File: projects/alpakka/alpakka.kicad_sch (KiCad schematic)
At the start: 56 parts, among them P1 Conn_01x20_Pin, P2 Conn_01x20_Pin, P3 Headers 4P IN, P4 Blade, P5 Jack 2.5mm, P6 Conn_01x02, U1 Alpsalpine_RKJXV, U10 ST_LSM6, U12 ST_LSM6, U2 Alpsalpine_RKJXV, U3 Alpsalpine_EC10E, U6 NXP_PCAL6416A, U8 NXP_PCAL6416A

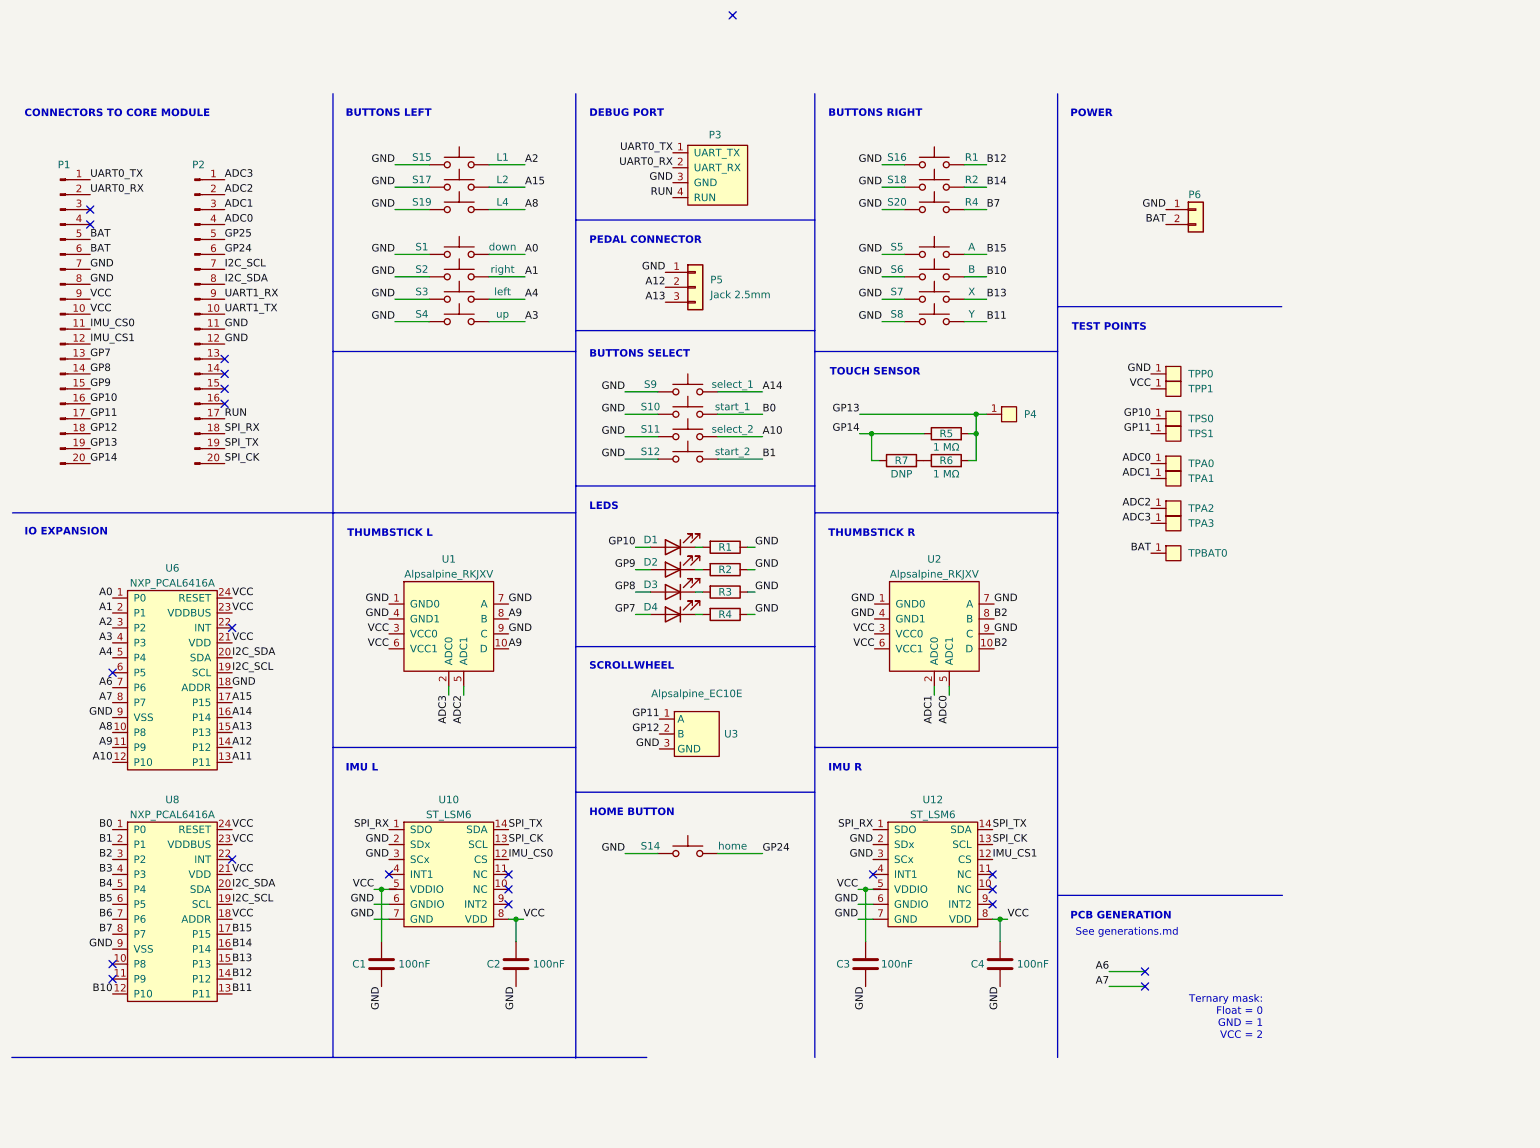
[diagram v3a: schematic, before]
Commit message: Alpakka added touch ref path, Reordered debug pins, Swapped analog 2-3, Removed wheel support holes, Added silkscreen
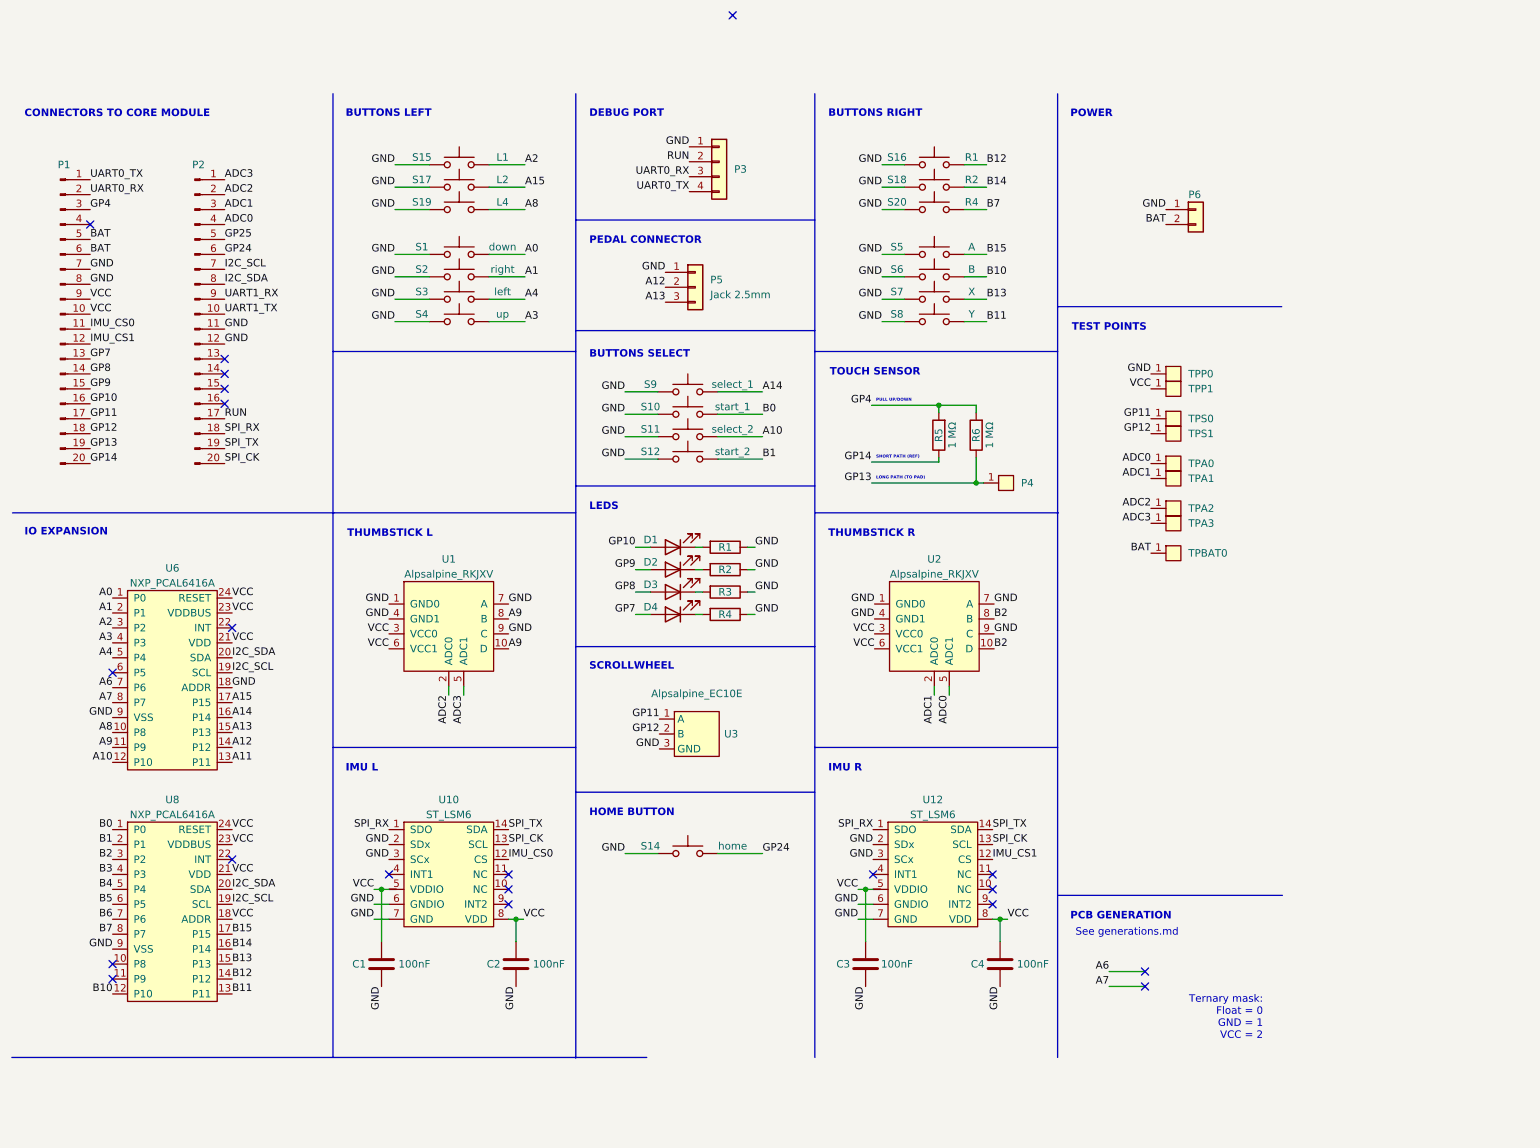
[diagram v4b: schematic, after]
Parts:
- removed P3: Headers 4P IN, ILO_fp:XKB_X6511FRS-04, symbol ILO_sym:Debug
- removed R7: DNP, ILO_fp:0603_compact, symbol Device:R
- added P3: Conn_01x04, ILO_fp:XKB_X6511FRS-04, symbol Connector_Generic:Conn_01x04
- renumbered R6 to R5, R5 to R6
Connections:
- net ADC2: now also U1.2 (ADC0); no longer U1.5 (ADC1)
- net ADC3: now also U1.5 (ADC1); no longer U1.2 (ADC0)
- net GND: now also P3.1 (Pin_1)
- net GP10: no longer TPS0.1
- net GP11: now also TPS0.1; no longer TPS1.1
- net GP12: now also TPS1.1
- net GP13: now also R6.1; no longer R5.2, R6.2
- net GP14: now also R5.1; no longer R6.1
- net RUN: now also P3.2 (Pin_2)
- net UART0_RX: now also P3.3 (Pin_3)
- net UART0_TX: now also P3.4 (Pin_4)
- net GP4: now reaches P1.3 (Pin_3)
- net GP4: now also R5.2, R6.2
- no-connect marks 22 -> 21
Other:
- note added: "LONG PATH (TO PAD)"
- note added: "PULL UP/DOWN"
- note added: "SHORT PATH (REF)"
- moved on the sheet: P4, R5, R6

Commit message: Alpakka revert to single touch path, Shifted GPIOs to match Marmota
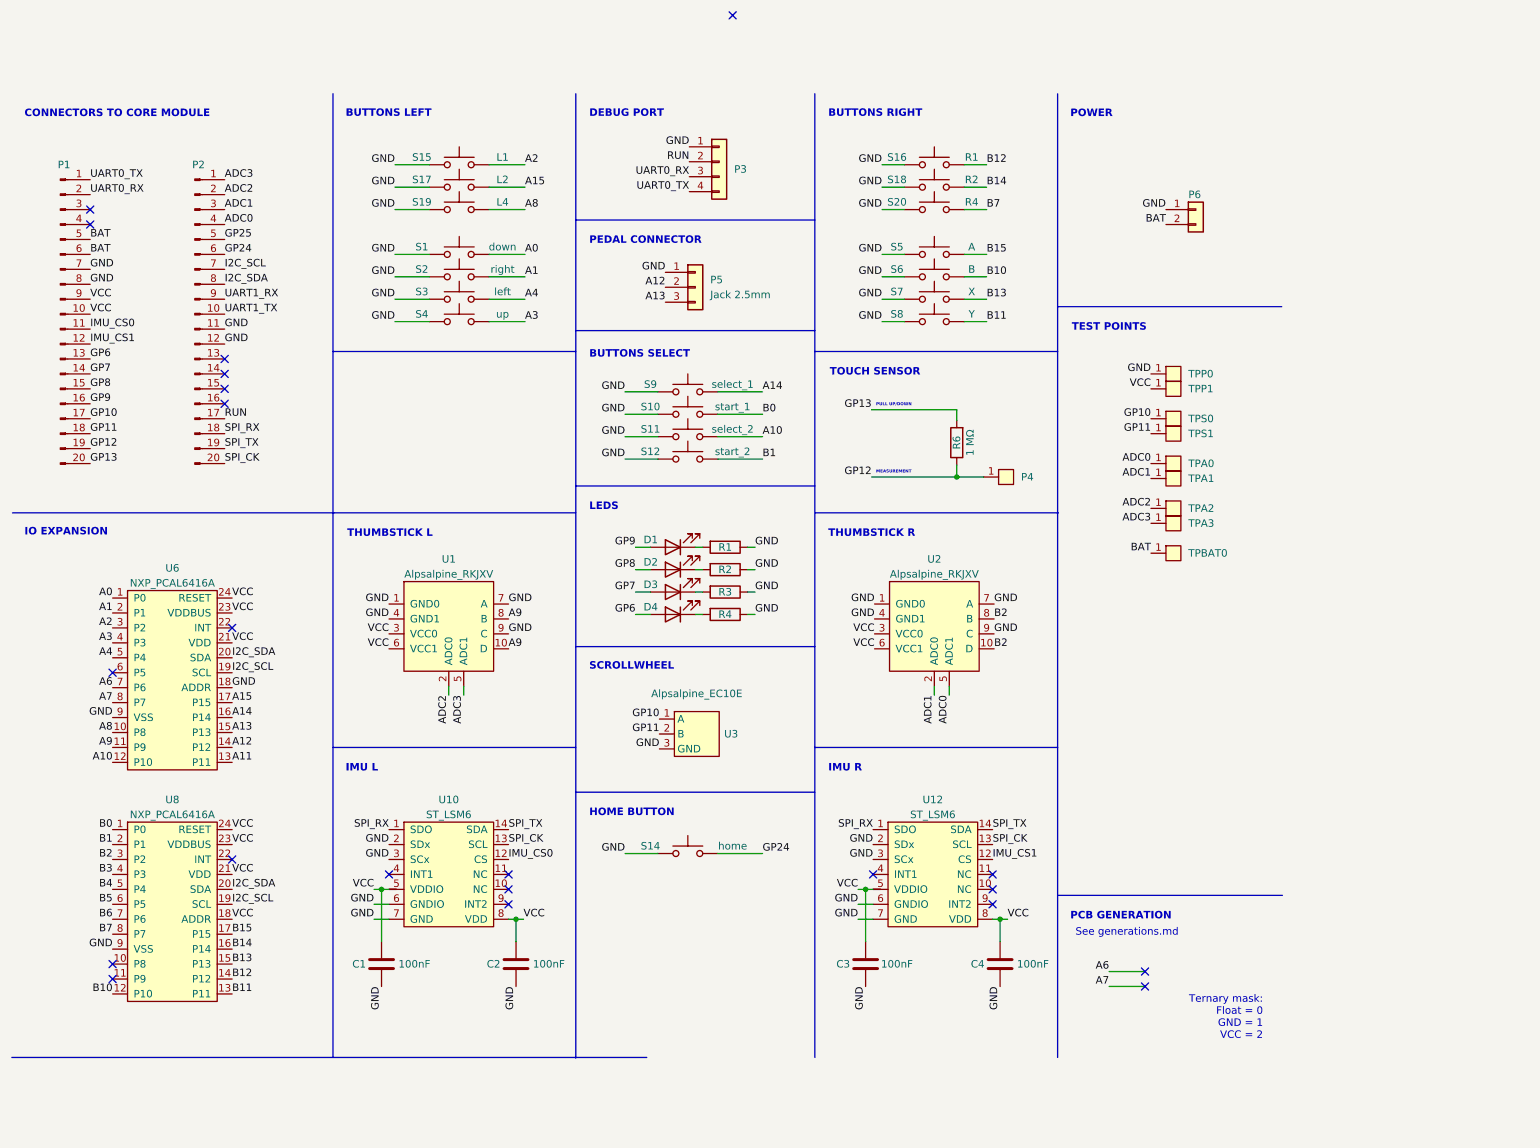
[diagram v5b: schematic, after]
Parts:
- removed R5: 1 MΩ, ILO_fp:0402, symbol Device:R
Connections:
- net GP14 is gone; now on net GP13: P1.20 (Pin_20)
- net GP10: now also P1.17 (Pin_17), TPS0.1, U3.1 (A); no longer D1.2 (A), P1.16 (Pin_16)
- net GP11: now also P1.18 (Pin_18), TPS1.1, U3.2 (B); no longer P1.17 (Pin_17), TPS0.1, U3.1 (A)
- net GP12: now also P1.19 (Pin_19), P4.1, R6.1; no longer P1.18 (Pin_18), TPS1.1, U3.2 (B)
- net GP13: now also R6.2; no longer P1.19 (Pin_19), P4.1, R6.1
- net GP7: now also D3.2 (A), P1.14 (Pin_14); no longer D4.2 (A), P1.13 (Pin_13)
- net GP8: now also D2.2 (A), P1.15 (Pin_15); no longer D3.2 (A), P1.14 (Pin_14)
- net GP9: now also D1.2 (A), P1.16 (Pin_16); no longer D2.2 (A), P1.15 (Pin_15)
- net GP4: no longer names the net of P1.3 (Pin_3)
- net GP4: no longer R6.2
- new net GP6: D4.2 (A), P1.13 (Pin_13)
- no-connect marks 21 -> 22
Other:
- note added: "MEASUREMENT"
- note removed: "LONG PATH (TO PAD)"
- note removed: "SHORT PATH (REF)"
- moved on the sheet: P4, R6

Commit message: Reworked Alpakka w/ interrupt lines, etc
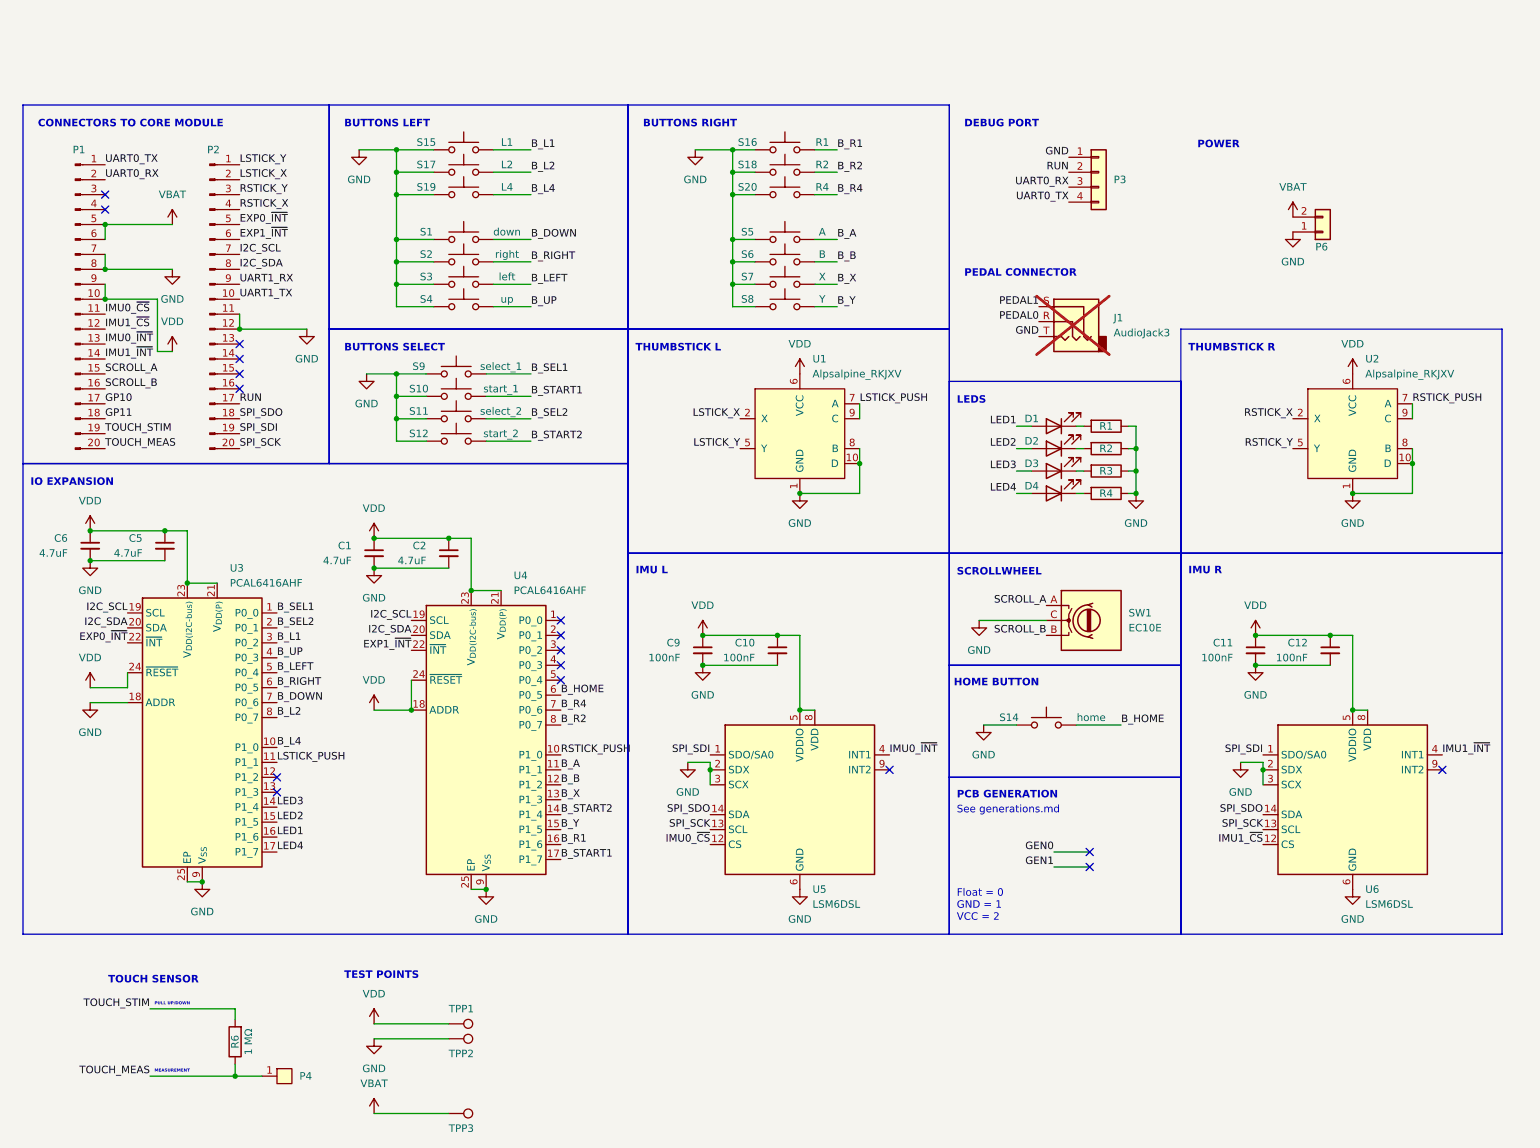
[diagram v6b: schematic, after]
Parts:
- removed C1, C2, C3, C4: 100nF, ILO_fp:0402, symbol Device:C
- removed P5: Jack 2.5mm, symbol Connector_Generic:Conn_01x03
- removed TPA0, TPA1, TPA2, TPA3, TPBAT0, TPP0, TPS0, TPS1: Endpoint, ILO_fp:Pad_1mm, symbol ILO_sym:Endpoint
- removed U10, U12: ST_LSM6, ILO_fp:LGA14, symbol ILO_sym:ST_LSM6
- removed U3: Alpsalpine_EC10E, ILO_fp:Alpsalpine_EC10E, symbol ILO_sym:Alpsalpine_EC10E
- removed U6, U8: NXP_PCAL6416A, ILO_fp:QFN24, symbol ILO_sym:NXP_PCAL6416A
- added C1, C2, C5, C6: 4.7uF, Capacitor_SMD:C_0603_1608Metric, symbol Device:C_Small
- added C10, C11, C12, C9: 100nF, Capacitor_SMD:C_0402_1005Metric, symbol Device:C_Small
- added J1: AudioJack3, Connector_Audio:Jack_3.5mm_CUI_SJ-3523-SMT_Horizontal, symbol Connector_Audio:AudioJack3
- added SW1: EC10E, ILO_fp:Alpsalpine_EC10E, symbol Device:RotaryEncoder
- added TPP2, TPP3: Endpoint, TestPoint:TestPoint_Pad_D1.0mm, symbol Connector:TestPoint
- added U3, U4: PCAL6416AHF, Package_DFN_QFN:HVQFN-24-1EP_4x4mm_P0.5mm_EP2.1x2.1mm, symbol Interface_Expansion:PCAL6416AHF
- added U5, U6: LSM6DSL, Package_LGA:LGA-14_3x2.5mm_P0.5mm_LayoutBorder3x4y, symbol Sensor_Motion:LSM6DSL
- D1, D2, D3, D4: footprint ILO_fp:0603_d -> Diode_SMD:D_0603_1608Metric
- P6: footprint ILO_fp:JST_PH_2_TH -> Connector_JST:JST_PH_S2B-PH-K_1x02_P2.00mm_Horizontal
- R1, R2, R3, R4: footprint ILO_fp:0603 -> Resistor_SMD:R_0603_1608Metric
- R6: footprint ILO_fp:0402 -> Resistor_SMD:R_0402_1005Metric
- TPP1: footprint ILO_fp:Pad_1mm -> TestPoint:TestPoint_Pad_D1.0mm; symbol ILO_sym:Endpoint -> Connector:TestPoint
- U1, U2: Export yes -> (none); Group Thumbstick -> (none); LCSC C918854 -> (none); Mount TH -> (none)
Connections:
- net A9 is gone; now on net GND: U1.10 (D), U1.8 (B)
- net B2 is gone; now on net GND: U2.10 (D), U2.8 (B)
- net GND: now also C1.2, C10.2, C11.2, C12.2, C2.2, C5.2, C6.2, C9.2, J1.T, SW1.C, TPP2.1, U3.18 (ADDR), U3.25 (EP), U3.9 (V_{SS}), U4.25 (EP), U4.9 (V_{SS}), U5.2 (SDX), U5.3 (SCX), U5.6 (GND), U5.7 (GND), U6.2 (SDX), U6.3 (SCX), U6.6 (GND), U6.7 (GND); no longer U1.7 (A), U1.9 (C), U2.7 (A), U2.9 (C)
- net I2C_SCL: now also U3.19 (SCL), U4.19 (SCL)
- net I2C_SDA: now also U3.20 (SDA), U4.20 (SDA)
- net A0 renamed B_DOWN
- net B_DOWN: now also U3.7 (P0_6)
- net A1 renamed B_RIGHT
- net B_RIGHT: now also U3.6 (P0_5)
- net A10 renamed B_SEL2
- net B_SEL2: now also U3.2 (P0_1)
- net A14 renamed B_SEL1
- net B_SEL1: now also U3.1 (P0_0)
- net A15 renamed B_L2
- net B_L2: now also U3.8 (P0_7)
- net A2 renamed B_L1
- net B_L1: now also U3.3 (P0_2)
- net A3 renamed B_UP
- net B_UP: now also U3.4 (P0_3)
- net A4 renamed B_LEFT
- net B_LEFT: now also U3.5 (P0_4)
- net A8 renamed B_L4
- net B_L4: now also U3.10 (P1_0)
- net ADC0 renamed RSTICK_X
- net RSTICK_X: now also U2.2 (X); no longer U2.5 (ADC1)
- net ADC1 renamed RSTICK_Y
- net RSTICK_Y: now also U2.5 (Y); no longer U2.2 (ADC0)
- net ADC2 renamed LSTICK_X
- net ADC3 renamed LSTICK_Y
- net B0 renamed B_START1
- net B_START1: now also U4.17 (P1_7)
- net B1 renamed B_START2
- net B_START2: now also U4.14 (P1_4)
- net B10 renamed B_B
- net B_B: now also U4.12 (P1_2)
- net B11 renamed B_Y
- net B_Y: now also U4.15 (P1_5)
- net B12 renamed B_R1
- net B_R1: now also U4.16 (P1_6)
- net B13 renamed B_X
- net B_X: now also U4.13 (P1_3)
- net B14 renamed B_R2
- net B_R2: now also U4.8 (P0_7)
- net B15 renamed B_A
- net B_A: now also U4.11 (P1_1)
- net B7 renamed B_R4
- net B_R4: now also U4.7 (P0_6)
- net BAT renamed VBAT
- net VBAT: now also TPP3.1
- net GP12 renamed TOUCH_MEAS
- net TOUCH_MEAS: now also P1.20 (Pin_20); no longer P1.19 (Pin_19)
- net GP13 renamed TOUCH_STIM
- net TOUCH_STIM: now also P1.19 (Pin_19); no longer P1.20 (Pin_20)
- net GP24 renamed B_HOME
- net B_HOME: now also U4.6 (P0_5); no longer P2.6 (Pin_6)
- net GP25 renamed EXP0_~{INT}
- net EXP0_~{INT}: now also U3.22 (~{INT})
- net GP6 renamed IMU0_~{INT}
- net IMU0_~{INT}: now also U5.4 (INT1); no longer D4.2 (A)
- net GP7 renamed IMU1_~{INT}
- net IMU1_~{INT}: now also U6.4 (INT1); no longer D3.2 (A)
- net GP8 renamed LED2
- net LED2: now also U3.15 (P1_5); no longer P1.15 (Pin_15)
- net GP9 renamed LED1
- net LED1: now also U3.16 (P1_6); no longer P1.16 (Pin_16)
- net IMU_CS0 renamed IMU0_~{CS}
- net IMU0_~{CS}: now also U5.12 (CS)
- net IMU_CS1 renamed IMU1_~{CS}
- net IMU1_~{CS}: now also U6.12 (CS)
- net SPI_CK renamed SPI_SCK
- net SPI_SCK: now also U5.13 (SCL), U6.13 (SCL)
- net SPI_RX renamed SPI_SDO
- net SPI_SDO: now also U5.14 (SDA), U6.14 (SDA)
- net SPI_TX renamed SPI_SDI
- net SPI_SDI: now also U5.1 (SDO/SA0), U6.1 (SDO/SA0)
- net VCC renamed VDD
- net VDD: now also C1.1, C10.1, C11.1, C12.1, C2.1, C5.1, C6.1, C9.1, U3.21 (V_{DD(P)}), U3.23 (V_{DD(I2C-bus)}), U3.24 (~{RESET}), U4.18 (ADDR), U4.21 (V_{DD(P)}), U4.23 (V_{DD(I2C-bus)}), U4.24 (~{RESET}), U5.5 (VDDIO), U5.8 (VDD), U6.5 (VDDIO), U6.8 (VDD)
- new net EXP1_~{INT}: P2.6 (Pin_6), U4.22 (~{INT})
- new net LED3: D3.2 (A), U3.14 (P1_4)
- new net LED4: D4.2 (A), U3.17 (P1_7)
- new net LSTICK_PUSH: U1.7 (A), U1.9 (C), U3.11 (P1_1)
- new net PEDAL0: J1.R
- new net PEDAL1: J1.S
- new net RSTICK_PUSH: U2.7 (A), U2.9 (C), U4.10 (P1_0)
- new net SCROLL_A: P1.15 (Pin_15), SW1.A
- new net SCROLL_B: P1.16 (Pin_16), SW1.B
- no-connect marks 22 -> 17
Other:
- note added: "Float = 0 GND = 1 VCC = 2"
- note removed: "Ternary mask: Float = 0 GND = 1 VCC = 2"
- moved on the sheet: D1, D2, D3, D4, P1, P2, P3, P4, P6, R1, R2, R3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
